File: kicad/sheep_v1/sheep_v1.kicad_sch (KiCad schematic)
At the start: 20 parts, among them J1 AudioJack4dpb, SW1 SW_Push, SW10 SW_Push, SW11 SW_Push, SW12 SW_Push, SW13 SW_Push, SW14 SW_Push, SW15 SW_Push, SW16 SW_Push, SW17 SW_Push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

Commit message: Add qmk files
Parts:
- U1: value ProMicro-kbd -> MicroController; footprint kbd:ProMicro_v2 -> RP2040
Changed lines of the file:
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@@
     (pin "2")
     (instances
-      (project "routes"
+      (project "enlarge_pads"
         (path "/1418ad6a-8a4d-429d-b07e-469b1ffa21a0"
           (reference "SW13") (unit 1)
@@
     (pin "2")
     (instances
-      (project "routes"
+      (project "enlarge_pads"
         (path "/1418ad6a-8a4d-429d-b07e-469b1ffa21a0"
           (reference "SW12") (unit 1)
@@
     (pin "2")
     (instances
-      (project "routes"
+      (project "enlarge_pads"
         (path "/1418ad6a-8a4d-429d-b07e-469b1ffa21a0"
           (reference "SW16") (unit 1)
@@
     (pin "2")
     (instances
-      (project "routes"
+      (project "enlarge_pads"
         (path "/1418ad6a-8a4d-429d-b07e-469b1ffa21a0"
           (reference "SW15") (unit 1)
@@
     (pin "2")
     (instances
-      (project "routes"
+      (project "enlarge_pads"
         (path "/1418ad6a-8a4d-429d-b07e-469b1ffa21a0"
           (reference "SW2") (unit 1)
@@
     (pin "D")
     (instances
-      (project "routes"
+      (project "enlarge_pads"
         (path "/1418ad6a-8a4d-429d-b07e-469b1ffa21a0"
           (reference "J1") (unit 1)
@@
     (pin "2")
     (instances
-      (project "routes"
+      (project "enlarge_pads"
         (path "/1418ad6a-8a4d-429d-b07e-469b1ffa21a0"
           (reference "SW14") (unit 1)
@@
     (pin "2")
     (instances
-      (project "routes"
+      (project "enlarge_pads"
         (path "/1418ad6a-8a4d-429d-b07e-469b1ffa21a0"
           (reference "SW4") (unit 1)
@@
     (pin "2")
     (instances
-      (project "routes"
+      (project "enlarge_pads"
         (path "/1418ad6a-8a4d-429d-b07e-469b1ffa21a0"
           (reference "SW1") (unit 1)
@@
     (pin "2")
     (instances
-      (project "routes"
+      (project "enlarge_pads"
         (path "/1418ad6a-8a4d-429d-b07e-469b1ffa21a0"
           (reference "SW3") (unit 1)
@@
     (pin "2")
     (instances
-      (project "routes"
+      (project "enlarge_pads"
         (path "/1418ad6a-8a4d-429d-b07e-469b1ffa21a0"
           (reference "SW5") (unit 1)
@@
     (pin "2")
     (instances
-      (project "routes"
+      (project "enlarge_pads"
         (path "/1418ad6a-8a4d-429d-b07e-469b1ffa21a0"
           (reference "SW9") (unit 1)
@@
       (effects (font (size 1.524 1.524)))
     )
-    (property "Value" "ProMicro-kbd" (at 231.14 35.8902 0)
+    (property "Value" "MicroController" (at 231.14 35.8902 0)
       (effects (font (size 1.524 1.524)))
     )
-    (property "Footprint" "kbd:ProMicro_v2" (at 231.14 38.5826 0)
+    (property "Footprint" "RP2040" (at 231.14 38.5826 0)
       (effects (font (size 1.524 1.524)))
     )
@@
     (pin "9")
     (instances
-      (project "routes"
+      (project "enlarge_pads"
         (path "/1418ad6a-8a4d-429d-b07e-469b1ffa21a0"
           (reference "U1") (unit 1)
@@
     (pin "2")
     (instances
-      (project "routes"
+      (project "enlarge_pads"
         (path "/1418ad6a-8a4d-429d-b07e-469b1ffa21a0"
           (reference "SW10") (unit 1)
@@
     (pin "2")
     (instances
-      (project "routes"
+      (project "enlarge_pads"
         (path "/1418ad6a-8a4d-429d-b07e-469b1ffa21a0"
           (reference "SW11") (unit 1)
@@
     (pin "2")
     (instances
-      (project "routes"
+      (project "enlarge_pads"
         (path "/1418ad6a-8a4d-429d-b07e-469b1ffa21a0"
           (reference "SW6") (unit 1)
@@
     (pin "2")
     (instances
-      (project "routes"
+      (project "enlarge_pads"
         (path "/1418ad6a-8a4d-429d-b07e-469b1ffa21a0"
           (reference "SW7") (unit 1)
@@
     (pin "2")
     (instances
-      (project "routes"
+      (project "enlarge_pads"
         (path "/1418ad6a-8a4d-429d-b07e-469b1ffa21a0"
           (reference "RSW1") (unit 1)
@@
     (pin "2")
     (instances
-      (project "routes"
+      (project "enlarge_pads"
         (path "/1418ad6a-8a4d-429d-b07e-469b1ffa21a0"
           (reference "SW17") (unit 1)
@@
     (pin "2")
     (instances
-      (project "routes"
+      (project "enlarge_pads"
         (path "/1418ad6a-8a4d-429d-b07e-469b1ffa21a0"
           (reference "SW8") (unit 1)

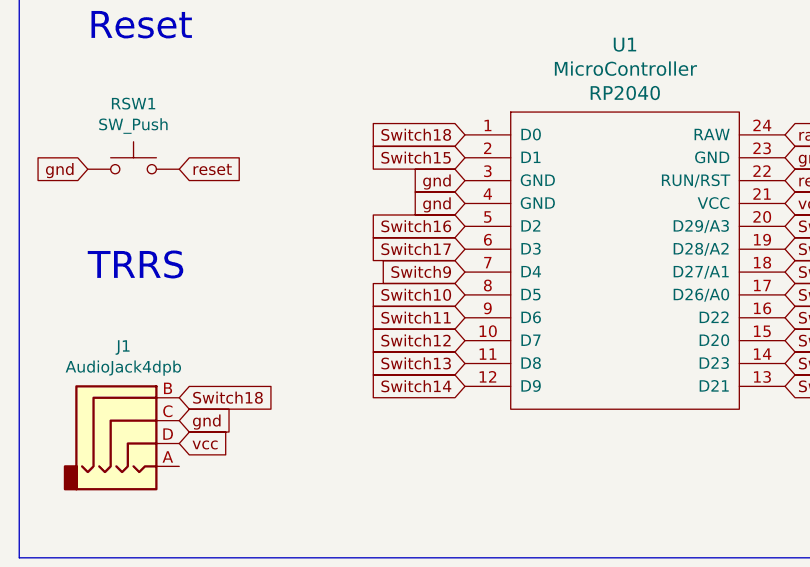
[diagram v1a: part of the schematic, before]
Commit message: Reversed controller ok + up matrix pins
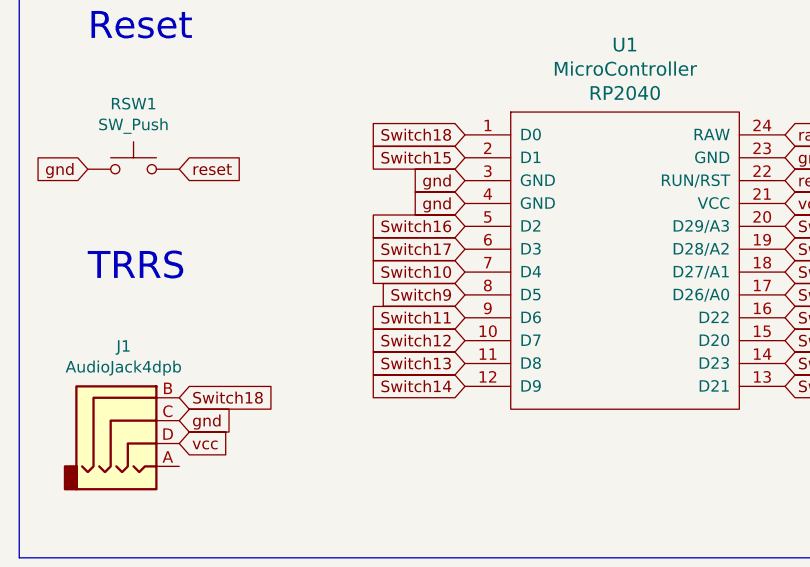
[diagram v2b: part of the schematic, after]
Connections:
- net Switch10: now also U1.7 (D4); no longer U1.8 (D5)
- net Switch9: now also U1.8 (D5); no longer U1.7 (D4)
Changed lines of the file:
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@@
     )
   )
-  (global_label "Switch9" (shape input) (at 213.36 58.42 180) (fields_autoplaced)
-    (effects (font (size 1.27 1.27)) (justify right))
-    (property "Intersheetrefs" "${INTERSHEET_REFS}" (at 203.7114 58.42 0)
+  (global_label "Switch10" (shape input) (at 213.36 58.42 180) (fields_autoplaced)
+    (effects (font (size 1.27 1.27)) (justify right))
+    (property "Intersheetrefs" "${INTERSHEET_REFS}" (at 202.5019 58.42 0)
       (effects (font (size 1.27 1.27)) (justify right) hide)
     )
@@
     )
   )
-  (global_label "Switch10" (shape input) (at 213.36 60.96 180) (fields_autoplaced)
-    (effects (font (size 1.27 1.27)) (justify right))
-    (property "Intersheetrefs" "${INTERSHEET_REFS}" (at 202.5019 60.96 0)
+  (global_label "Switch9" (shape input) (at 213.36 60.96 180) (fields_autoplaced)
+    (effects (font (size 1.27 1.27)) (justify right))
+    (property "Intersheetrefs" "${INTERSHEET_REFS}" (at 203.7114 60.96 0)
       (effects (font (size 1.27 1.27)) (justify right) hide)
     )
@@
     (pin "2")
     (instances
-      (project "enlarge_pads"
+      (project "test_reverse_controller"
         (path "/1418ad6a-8a4d-429d-b07e-469b1ffa21a0"
           (reference "SW13") (unit 1)
@@
     (pin "2")
     (instances
-      (project "enlarge_pads"
+      (project "test_reverse_controller"
         (path "/1418ad6a-8a4d-429d-b07e-469b1ffa21a0"
           (reference "SW12") (unit 1)
@@
     (pin "2")
     (instances
-      (project "enlarge_pads"
+      (project "test_reverse_controller"
         (path "/1418ad6a-8a4d-429d-b07e-469b1ffa21a0"
           (reference "SW16") (unit 1)
@@
     (pin "2")
     (instances
-      (project "enlarge_pads"
+      (project "test_reverse_controller"
         (path "/1418ad6a-8a4d-429d-b07e-469b1ffa21a0"
           (reference "SW15") (unit 1)
@@
     (pin "2")
     (instances
-      (project "enlarge_pads"
+      (project "test_reverse_controller"
         (path "/1418ad6a-8a4d-429d-b07e-469b1ffa21a0"
           (reference "SW2") (unit 1)
@@
     (pin "D")
     (instances
-      (project "enlarge_pads"
+      (project "test_reverse_controller"
         (path "/1418ad6a-8a4d-429d-b07e-469b1ffa21a0"
           (reference "J1") (unit 1)
@@
     (pin "2")
     (instances
-      (project "enlarge_pads"
+      (project "test_reverse_controller"
         (path "/1418ad6a-8a4d-429d-b07e-469b1ffa21a0"
           (reference "SW14") (unit 1)
@@
     (pin "2")
     (instances
-      (project "enlarge_pads"
+      (project "test_reverse_controller"
         (path "/1418ad6a-8a4d-429d-b07e-469b1ffa21a0"
           (reference "SW4") (unit 1)
@@
     (pin "2")
     (instances
-      (project "enlarge_pads"
+      (project "test_reverse_controller"
         (path "/1418ad6a-8a4d-429d-b07e-469b1ffa21a0"
           (reference "SW1") (unit 1)
@@
     (pin "2")
     (instances
-      (project "enlarge_pads"
+      (project "test_reverse_controller"
         (path "/1418ad6a-8a4d-429d-b07e-469b1ffa21a0"
           (reference "SW3") (unit 1)
@@
     (pin "2")
     (instances
-      (project "enlarge_pads"
+      (project "test_reverse_controller"
         (path "/1418ad6a-8a4d-429d-b07e-469b1ffa21a0"
           (reference "SW5") (unit 1)
@@
     (pin "2")
     (instances
-      (project "enlarge_pads"
+      (project "test_reverse_controller"
         (path "/1418ad6a-8a4d-429d-b07e-469b1ffa21a0"
           (reference "SW9") (unit 1)
@@
     (pin "9")
     (instances
-      (project "enlarge_pads"
+      (project "test_reverse_controller"
         (path "/1418ad6a-8a4d-429d-b07e-469b1ffa21a0"
           (reference "U1") (unit 1)
@@
     (pin "2")
     (instances
-      (project "enlarge_pads"
+      (project "test_reverse_controller"
         (path "/1418ad6a-8a4d-429d-b07e-469b1ffa21a0"
           (reference "SW10") (unit 1)
@@
     (pin "2")
     (instances
-      (project "enlarge_pads"
+      (project "test_reverse_controller"
         (path "/1418ad6a-8a4d-429d-b07e-469b1ffa21a0"
           (reference "SW11") (unit 1)
@@
     (pin "2")
     (instances
-      (project "enlarge_pads"
+      (project "test_reverse_controller"
         (path "/1418ad6a-8a4d-429d-b07e-469b1ffa21a0"
           (reference "SW6") (unit 1)
@@
     (pin "2")
     (instances
-      (project "enlarge_pads"
+      (project "test_reverse_controller"
         (path "/1418ad6a-8a4d-429d-b07e-469b1ffa21a0"
           (reference "SW7") (unit 1)
@@
     (pin "2")
     (instances
-      (project "enlarge_pads"
+      (project "test_reverse_controller"
         (path "/1418ad6a-8a4d-429d-b07e-469b1ffa21a0"
           (reference "RSW1") (unit 1)
@@
     (pin "2")
     (instances
-      (project "enlarge_pads"
+      (project "test_reverse_controller"
         (path "/1418ad6a-8a4d-429d-b07e-469b1ffa21a0"
           (reference "SW17") (unit 1)
@@
     (pin "2")
     (instances
-      (project "enlarge_pads"
+      (project "test_reverse_controller"
         (path "/1418ad6a-8a4d-429d-b07e-469b1ffa21a0"
           (reference "SW8") (unit 1)
